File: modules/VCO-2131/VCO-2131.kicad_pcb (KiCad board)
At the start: 2 copper layers, 167.3 x 108.2 mm, 108 parts, among them J1 WQP-PJ398, J10 Conn_Front_Left, J11 Conn_Front_Right, J12 Conn_Back_Right, J13 Conn_Back_Left, J14 Conn_Passthru_Right, J15 Conn_Passthru_Left, J16 Conn_Mid_Right, J17 Conn_Mid_Left, J2 WQP-PJ398, J3 WQP-PJ398, J4 WQP-PJ398, J5 WQP-PJ398, J6 WQP-PJ398, J7 WQP-PJ398, J8 WQP-PJ398, J9 Conn_Eurorack_16, SW5 ON_OFF_ON, U1 L78L05, U2 L79L05, U3 LM4040, U4 SSI2131, U5 TL074, U6 TL074, U7 TL074, U8 CD4013

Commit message: VCO-2131: PCB layout tweaks
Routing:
- net VREF+: track 337.6 -> 337.1 mm
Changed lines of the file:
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@@
   (segment (start 170.053 46.609) (end 174.752 51.308) (width 0.381) (layer "F.Cu") (net 7))
   (segment (start 178.896 51.308) (end 174.752 51.308) (width 0.381) (layer "F.Cu") (net 7))
-  (segment (start 59.4106 96.5454) (end 59.4106 96.52) (width 0.381) (layer "F.Cu") (net 11))
-  (segment (start 49.276 106.68) (end 59.4106 96.5454) (width 0.381) (layer "F.Cu") (net 11))
+  (segment (start 59.436 96.52) (end 49.276 106.68) (width 0.381) (layer "F.Cu") (net 11))
   (segment (start 83.82 88.9) (end 86.36 88.9) (width 0.762) (layer "F.Cu") (net 11))
   (segment (start 88.773 90.551) (end 87.122 88.9) (width 0.381) (layer "F.Cu") (net 11))
@@
   (segment (start 93.599 96.52) (end 91.821 96.52) (width 0.381) (layer "F.Cu") (net 11))
   (segment (start 163.957 97.155) (end 163.957 101.346) (width 0.381) (layer "F.Cu") (net 11))
+  (segment (start 61.468 96.52) (end 59.436 96.52) (width 0.381) (layer "F.Cu") (net 11))
   (segment (start 87.122 88.9) (end 86.36 88.9) (width 0.381) (layer "F.Cu") (net 11))
   (segment (start 88.773 93.472) (end 88.773 90.551) (width 0.381) (layer "F.Cu") (net 11))
-  (via (at 59.4106 96.52) (size 0.8) (drill 0.4) (layers "F.Cu" "B.Cu") (net 11))
+  (via (at 61.468 96.52) (size 0.8) (drill 0.4) (layers "F.Cu" "B.Cu") (net 11))
   (segment (start 144.78 88.9) (end 151.511 88.9) (width 0.381) (layer "B.Cu") (net 11))
-  (segment (start 59.4106 96.52) (end 64.5922 96.52) (width 0.381) (layer "B.Cu") (net 11))
-  (segment (start 72.2122 88.9) (end 73.36 88.9) (width 0.381) (layer "B.Cu") (net 11))
   (segment (start 64.5922 96.52) (end 72.2122 88.9) (width 0.381) (layer "B.Cu") (net 11))
   (segment (start 151.511 88.9) (end 163.957 101.346) (width 0.381) (layer "B.Cu") (net 11))
-  (segment (start 53.2638 107.8738) (end 45.0088 116.1288) (width 0.381) (layer "F.Cu") (net 12))
-  (segment (start 60.071 100.9015) (end 57.1119 100.9015) (width 0.381) (layer "F.Cu") (net 12))
+  (segment (start 72.2122 88.9) (end 73.36 88.9) (width 0.381) (layer "B.Cu") (net 11))
+  (segment (start 61.468 96.52) (end 64.5922 96.52) (width 0.381) (layer "B.Cu") (net 11))
+  (segment (start 41.0718 121.1326) (end 40.2082 120.269) (width 0.381) (layer "F.Cu") (net 12))
   (segment (start 45.0088 116.1288) (end 45.0088 120.3452) (width 0.381) (layer "F.Cu") (net 12))
-  (segment (start 57.1119 100.9015) (end 53.2638 104.7496) (width 0.381) (layer "F.Cu") (net 12))
   (segment (start 150.368 112.268) (end 146.685 108.585) (width 0.381) (layer "F.Cu") (net 12))
   (segment (start 153.1493 112.268) (end 150.368 112.268) (width 0.381) (layer "F.Cu") (net 12))
   (segment (start 154.432 113.5507) (end 153.1493 112.268) (width 0.381) (layer "F.Cu") (net 12))
+  (segment (start 59.944 102.489) (end 55.5244 102.489) (width 0.381) (layer "F.Cu") (net 12))
+  (segment (start 146.685 95.885) (end 144.78 93.98) (width 0.381) (layer "F.Cu") (net 12))
+  (segment (start 53.2638 104.7496) (end 53.2638 107.8738) (width 0.381) (layer "F.Cu") (net 12))
   (segment (start 45.0088 120.3452) (end 44.2214 121.1326) (width 0.381) (layer "F.Cu") (net 12))
-  (segment (start 53.2638 104.7496) (end 53.2638 107.8738) (width 0.381) (layer "F.Cu") (net 12))
-  (segment (start 146.685 95.885) (end 144.78 93.98) (width 0.381) (layer "F.Cu") (net 12))
+  (segment (start 53.2638 107.8738) (end 45.0088 116.1288) (width 0.381) (layer "F.Cu") (net 12))
   (segment (start 155.956 116.586) (end 154.432 115.062) (width 0.381) (layer "F.Cu") (net 12))
   (segment (start 83.82 93.98) (end 86.36 93.98) (width 0.762) (layer "F.Cu") (net 12))
   (segment (start 156.337 116.586) (end 155.956 116.586) (width 0.381) (layer "F.Cu") (net 12))
+  (segment (start 40.2082 120.269) (end 36.576 120.269) (width 0.381) (layer "F.Cu") (net 12))
+  (segment (start 55.5244 102.489) (end 53.2638 104.7496) (width 0.381) (layer "F.Cu") (net 12))
   (segment (start 146.685 108.585) (end 146.685 95.885) (width 0.381) (layer "F.Cu") (net 12))
-  (segment (start 40.2082 120.269) (end 36.576 120.269) (width 0.381) (layer "F.Cu") (net 12))
-  (segment (start 41.0718 121.1326) (end 40.2082 120.269) (width 0.381) (layer "F.Cu") (net 12))
   (segment (start 44.2214 121.1326) (end 41.0718 121.1326) (width 0.381) (layer "F.Cu") (net 12))
   (segment (start 154.432 115.062) (end 154.432 113.5507) (width 0.381) (layer "F.Cu") (net 12))
-  (via (at 60.071 100.9015) (size 0.8) (drill 0.4) (layers "F.Cu" "B.Cu") (net 12))
+  (via (at 59.944 102.489) (size 0.8) (drill 0.4) (layers "F.Cu" "B.Cu") (net 12))
   (segment (start 152.4 120.523) (end 156.337 116.586) (width 0.381) (layer "B.Cu") (net 12))
-  (segment (start 60.071 100.9015) (end 66.4385 100.9015) (width 0.381) (layer "B.Cu") (net 12))
-  (segment (start 66.4385 100.9015) (end 73.36 93.98) (width 0.381) (layer "B.Cu") (net 12))
+  (segment (start 59.944 102.489) (end 64.851 102.489) (width 0.381) (layer "B.Cu") (net 12))
+  (segment (start 64.851 102.489) (end 73.36 93.98) (width 0.381) (layer "B.Cu") (net 12))
   (segment (start 152.4 121.666) (end 152.4 120.523) (width 0.381) (layer "B.Cu") (net 12))
   (segment (start 55.8546 114.8334) (end 54.7116 114.8334) (width 0.381) (layer "F.Cu") (net 13))
@@
   (segment (start 174.234 72.898) (end 171.694 75.438) (width 0.762) (layer "F.Cu") (net 28))
   (segment (start 29.083 39.37) (end 33.909 34.544) (width 0.762) (layer "F.Cu") (net 28))
-  (segment (start 145.161 118.999) (end 145.161 121.666) (width 0.762) (layer "F.Cu") (net 28))
   (segment (start 165.1 118.999) (end 173 111.099) (width 0.762) (layer "F.Cu") (net 28))
   (segment (start 48.387 53.34) (end 55.372 53.34) (width 0.762) (layer "F.Cu") (net 28))
-  (segment (start 145.161 118.999) (end 143.129 116.967) (width 0.762) (layer "F.Cu") (net 28))
-  (segment (start 143.129 107.315) (end 144.78 105.664) (width 0.762) (layer "F.Cu") (net 28))
+  (segment (start 143.256 114.681) (end 143.256 107.188) (width 0.762) (layer "F.Cu") (net 28))
   (segment (start 164.099 118.999) (end 165.1 118.999) (width 0.762) (layer "F.Cu") (net 28))
   (segment (start 45.847 55.88) (end 40.34 55.88) (width 0.762) (layer "F.Cu") (net 28))
@@
   (segment (start 121.92 76.073) (end 124.333 73.66) (width 0.762) (layer "F.Cu") (net 28))
   (segment (start 182.245 78.486) (end 179.324 78.486) (width 0.762) (layer "F.Cu") (net 28))
-  (segment (start 158.1 118.999) (end 145.161 118.999) (width 0.762) (layer "F.Cu") (net 28))
+  (segment (start 147.574 118.999) (end 147.574 119.253) (width 0.762) (layer "F.Cu") (net 28))
   (segment (start 173 103.541) (end 174.941 101.6) (width 0.762) (layer "F.Cu") (net 28))
   (segment (start 187.071 73.66) (end 182.245 78.486) (width 0.762) (layer "F.Cu") (net 28))
   (segment (start 174.941 93.0925) (end 177.673 90.3605) (width 0.762) (layer "F.Cu") (net 28))
   (segment (start 187.66 73.66) (end 187.071 73.66) (width 0.762) (layer "F.Cu") (net 28))
+  (segment (start 143.256 107.188) (end 144.78 105.664) (width 0.762) (layer "F.Cu") (net 28))
   (segment (start 38.608 34.544) (end 40.34 36.276) (width 0.762) (layer "F.Cu") (net 28))
-  (segment (start 143.129 116.967) (end 143.129 107.315) (width 0.762) (layer "F.Cu") (net 28))
   (segment (start 171.694 77.968) (end 175.768 82.042) (width 0.762) (layer "F.Cu") (net 28))
+  (segment (start 158.1 118.999) (end 147.574 118.999) (width 0.762) (layer "F.Cu") (net 28))
+  (segment (start 147.574 119.253) (end 145.161 121.666) (width 0.762) (layer "F.Cu") (net 28))
+  (segment (start 147.574 118.999) (end 143.256 114.681) (width 0.762) (layer "F.Cu") (net 28))
   (segment (start 48.387 53.34) (end 45.847 55.88) (width 0.762) (layer "F.Cu") (net 28))
   (segment (start 177.673 90.3605) (end 177.673 83.947) (width 0.762) (layer "F.Cu") (net 28))

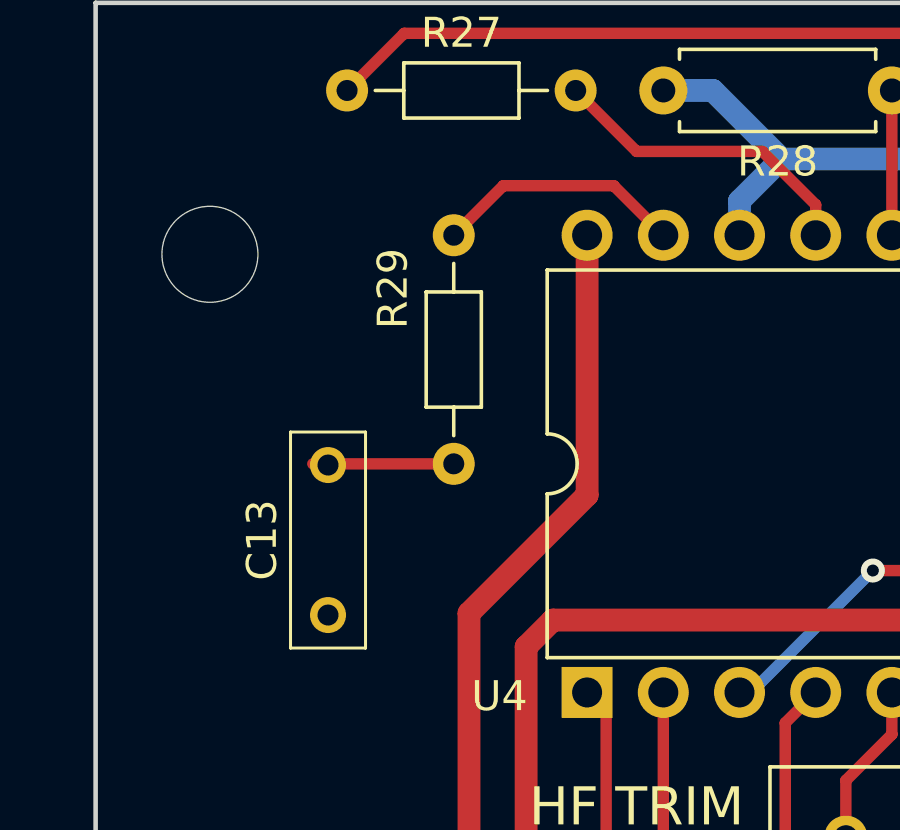
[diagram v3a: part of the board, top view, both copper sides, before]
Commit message: VCO-2131: PCB layout tweaks
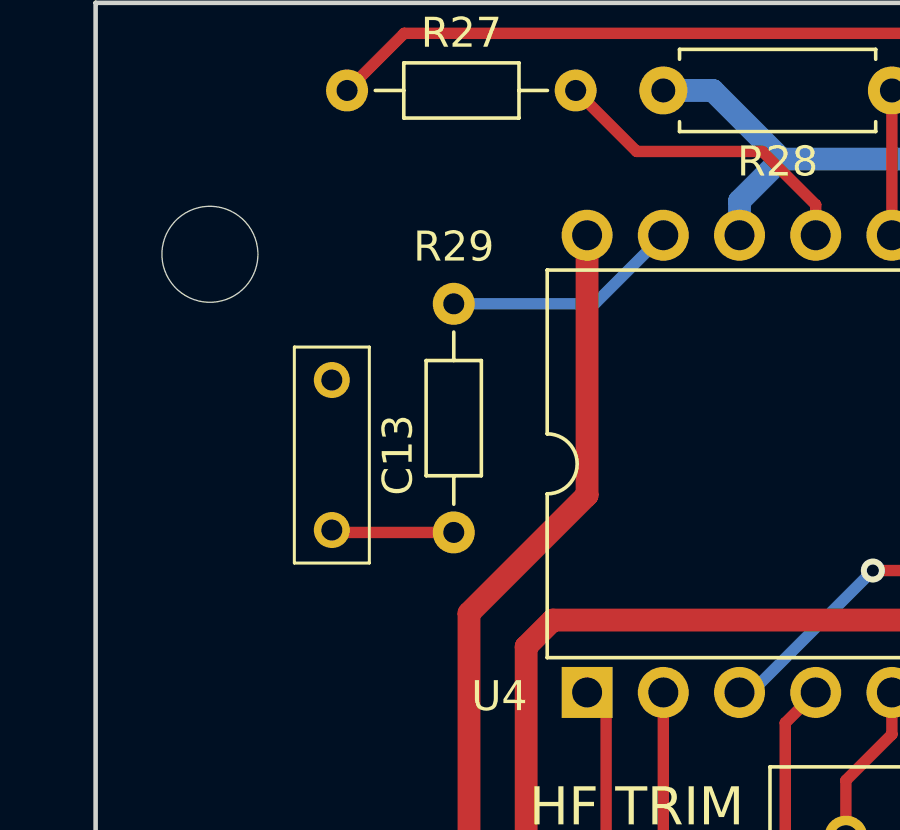
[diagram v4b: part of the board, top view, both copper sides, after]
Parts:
- moved C13 7.84 mm to (148.8, 51.4), turned to -90 degrees
- moved R29 2.29 mm to (152.9, 48.9)
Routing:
- net Net-(C13-Pad2): track 4.70 -> 4.10 mm
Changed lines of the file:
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@@
   )
   (footprint "-lmp-misc:R_Axial_DIN0204_L3.6mm_D1.6mm_P7.62mm_Horizontal" (layer "F.Cu")
-    (at 152.908 46.609 -90)
+    (at 152.908 48.895 -90)
     (descr "Resistor, Axial_DIN0204 series, Axial, Horizontal, pin pitch=7.62mm, 0.167W, length*diameter=3.6*1.6mm^2, http://cdn-reichelt.de/documents/datenblatt/B400/1_4W%23YAG.pdf")
     (tags "Resistor Axial_DIN0204 series Axial Horizontal pin pitch 7.62mm 0.167W length 3.6mm diameter 1.6mm")
@@
     (property "Value2" "1%, 1/6 W")
     (attr through_hole)
-    (fp_text reference "R29" (at 1.778 2.032 -90) (layer "F.SilkS")
+    (fp_text reference "R29" (at -1.905 0) (layer "F.SilkS")
       (effects (font (size 1 1) (thickness 0.15)))
     )
@@
   )
   (footprint "-lmp-misc:C_Rect_Kemet_L7.2mm_W2.5mm_P5mm" (layer "F.Cu")
-    (at 148.717 59.269 90)
+    (at 148.844 51.435 -90)
     (descr "MMK5223J50J01L4BULK-2")
     (tags "Capacitor")
@@
     (fp_line (start 6.1 1.25) (end -1.1 1.25) (layer "F.Fab") (width 0.2))
     (fp_line (start -1.1 -1.25) (end 6.1 -1.25) (layer "F.Fab") (width 0.2))
-    (pad "1" thru_hole circle locked (at 0 0 90) (size 1.2 1.2) (drill 0.7) (layers *.Cu *.Mask)
+    (pad "1" thru_hole circle locked (at 0 0 270) (size 1.2 1.2) (drill 0.7) (layers *.Cu *.Mask)
       (net 2 "GND") (pintype "passive"))
-    (pad "2" thru_hole circle locked (at 5 0 90) (size 1.2 1.2) (drill 0.7) (layers *.Cu *.Mask)
+    (pad "2" thru_hole circle locked (at 5 0 270) (size 1.2 1.2) (drill 0.7) (layers *.Cu *.Mask)
       (net 40 "Net-(C13-Pad2)") (pintype "passive"))
     (model "C:\\Users\\Len\\OneDrive\\Documents\\Electronics\\KiCad\\download\\SamacSys_Parts.3dshapes\\MMK5223J50J01L4BULK.stp"
@@
   (segment (start 170.678 72.898) (end 166.995 69.215) (width 0.381) (layer "F.Cu") (net 30))
   (segment (start 167.513 46.609) (end 167.513 41.783) (width 0.381) (layer "F.Cu") (net 31))
-  (segment (start 159.893 46.609) (end 158.242 44.958) (width 0.381) (layer "F.Cu") (net 32))
-  (segment (start 154.559 44.958) (end 152.908 46.609) (width 0.381) (layer "F.Cu") (net 32))
-  (segment (start 158.242 44.958) (end 154.559 44.958) (width 0.381) (layer "F.Cu") (net 32))
+  (segment (start 152.908 48.895) (end 157.607 48.895) (width 0.381) (layer "B.Cu") (net 32))
+  (segment (start 157.607 48.895) (end 159.893 46.609) (width 0.381) (layer "B.Cu") (net 32))
   (segment (start 150.368 72.771) (end 148.6535 74.4855) (width 0.381) (layer "F.Cu") (net 33))
   (segment (start 148.6535 94.2975) (end 148.6535 74.4855) (width 0.381) (layer "F.Cu") (net 33))
@@
   (segment (start 100.203 50.8) (end 101.6 49.403) (width 0.381) (layer "F.Cu") (net 39))
   (segment (start 92.583 47.244) (end 92.583 42.545) (width 0.381) (layer "B.Cu") (net 39))
-  (segment (start 152.908 54.229) (end 148.209 54.229) (width 0.381) (layer "F.Cu") (net 40))
+  (segment (start 152.908 56.515) (end 148.924 56.515) (width 0.381) (layer "F.Cu") (net 40))
+  (segment (start 148.924 56.515) (end 148.844 56.435) (width 0.381) (layer "F.Cu") (net 40))
   (segment (start 179.197 61.849) (end 175.133 61.849) (width 0.381) (layer "F.Cu") (net 41))
   (segment (start 185.247 101.6) (end 187.787 101.6) (width 0.762) (layer "F.Cu") (net 42))
